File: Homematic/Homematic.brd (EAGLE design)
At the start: 99.2 x 85 mm, 28 parts, among them IC1 3.3V, IC2 3.3V, P1 DF11-06-2DS, Q1 BS170

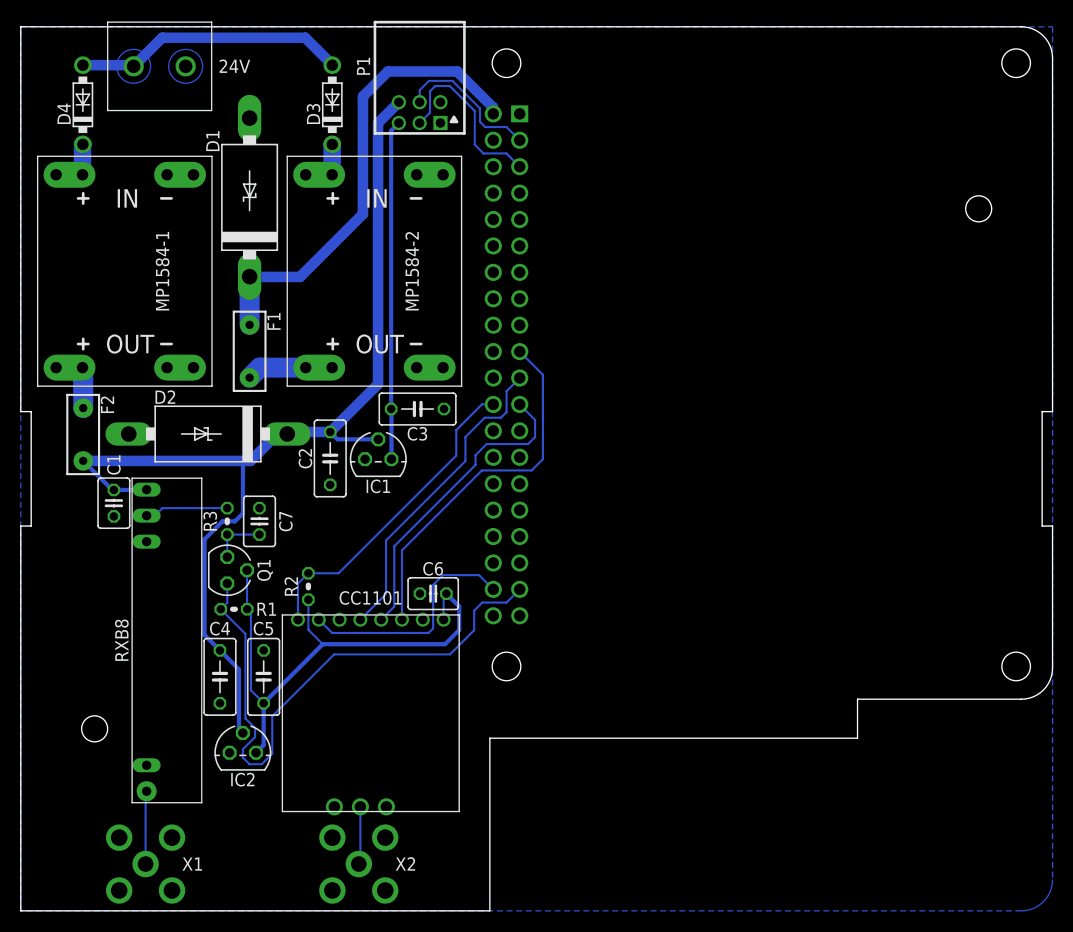
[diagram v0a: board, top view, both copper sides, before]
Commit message: Replace package for CC1101 receiver
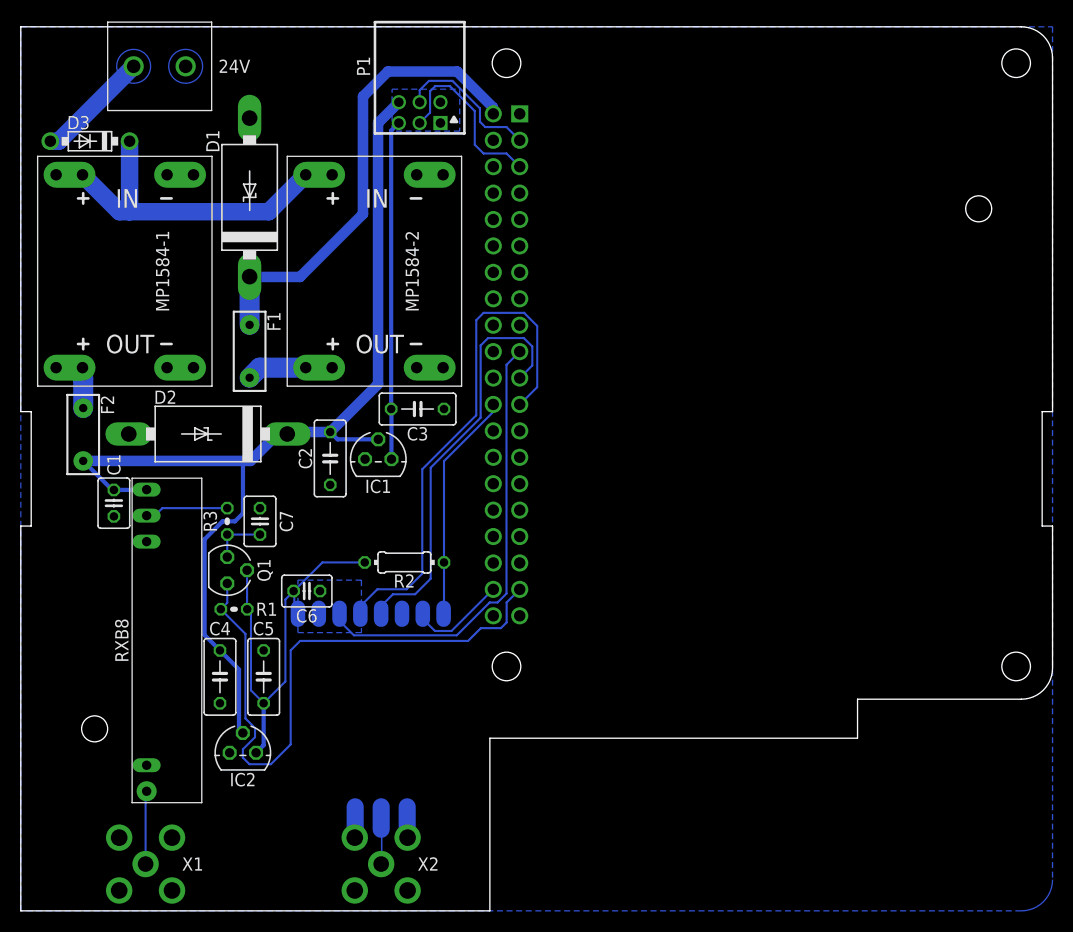
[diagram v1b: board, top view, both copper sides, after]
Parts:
- removed D4: SB1H100, diode:DO41-7.6
- CC1101: value CC1101 -> CC1101SMD; device modules:CC1101 -> modules:CC1101-SMD
- D3: value SB1H100 -> SB2H100
- R2: device rcl:0204V -> rcl:0204/7
- moved D3 23.6 mm to (6.65, 72.5), turned to 180 degrees
- moved C6 12.2 mm to (27.5, 29.2), turned to 0 degrees
- moved R2 9.51 mm to (36.9, 32.0), turned to 180 degrees
- moved X2 2.15 mm to (34.6, 3.00)
- moved C7 0.05 mm to (23.0, 36.0)
- flipped CC1101 to the bottom
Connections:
- removed net N$9: D4.C, MP1584-1.IN+0, MP1584-1.IN+1
- net +24V: no longer D4.A
- net N$7: now also MP1584-1.IN+0, MP1584-1.IN+1
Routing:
- net N$7: track 2.92 -> 31.2 mm
- net N$16: track 29.8 -> 49.5 mm
- net +24V: track 26.3 -> 11.0 mm
- net N$19: track 22.6 -> 9.49 mm
- net +3V3: track 51.7 -> 41.5 mm
- net N$17: track 30.5 -> 40.2 mm
- net N$15: track 30.8 -> 22.2 mm
- net N$18: track 35.1 -> 42.9 mm
- net N$10: track 55.9 -> 59.1 mm
- net N$9: track 2.93 -> 0.00 mm
- net N$20: track 5.56 -> 4.51 mm

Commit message: Change some routes
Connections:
- net N$10: now also RPI.40; no longer RPI.37
- net N$19: now also RPI.32; no longer RPI.38
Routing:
- net N$16: track 49.5 -> 40.9 mm
- net N$19: track 9.49 -> 17.3 mm
- net N$18: track 42.9 -> 48.2 mm
- net N$10: track 59.1 -> 54.0 mm
- net N$17: track 40.2 -> 37.1 mm
- net +3V3: track 41.5 -> 43.8 mm

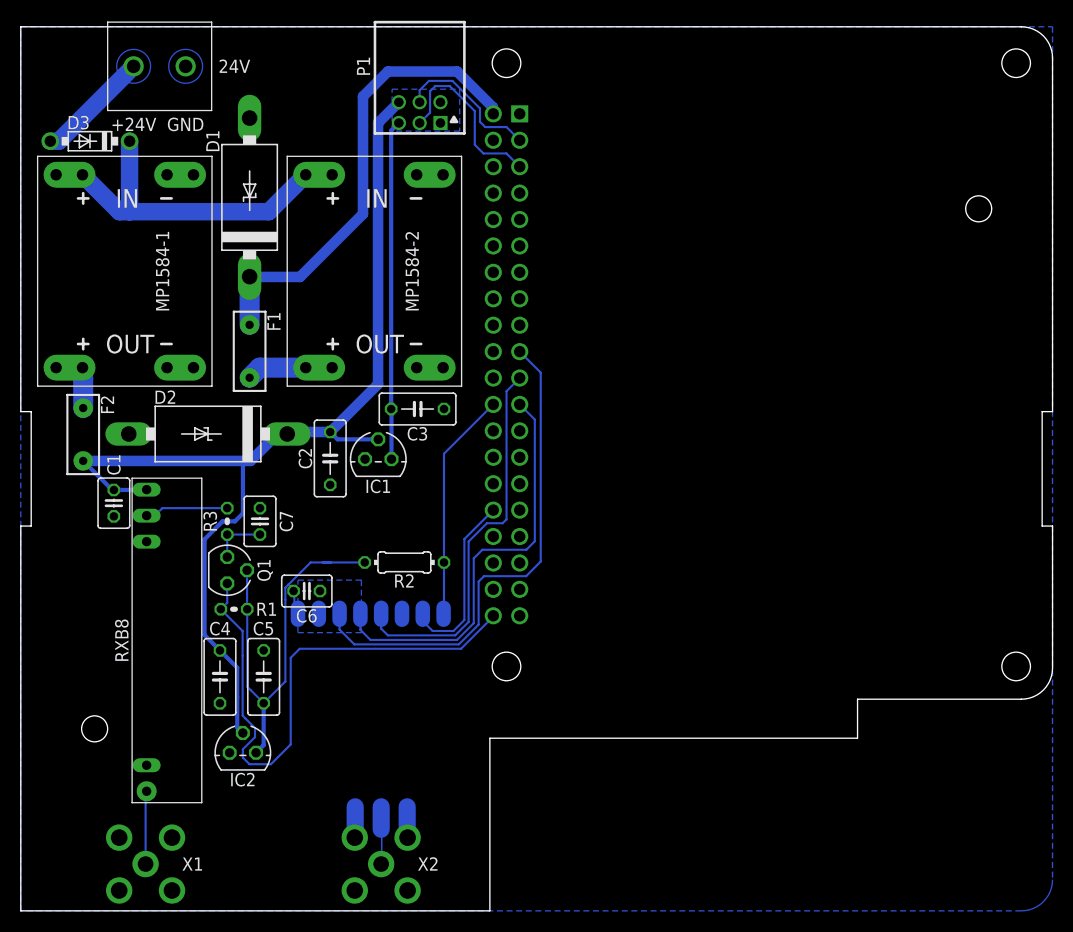
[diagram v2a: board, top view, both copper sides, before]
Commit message: Add top ground plate.
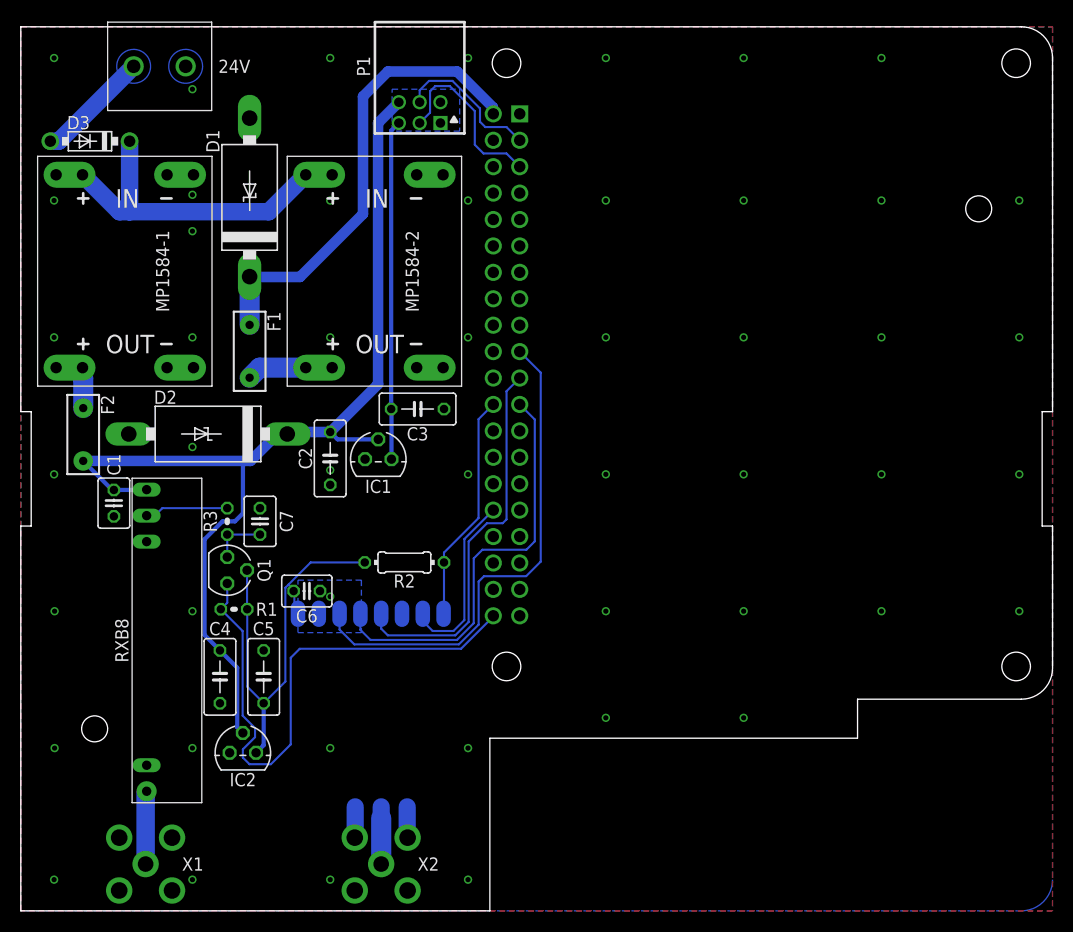
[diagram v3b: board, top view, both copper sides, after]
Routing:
- net +3V3: track 43.8 -> 42.9 mm
- added copper zone on layer 1, net GND

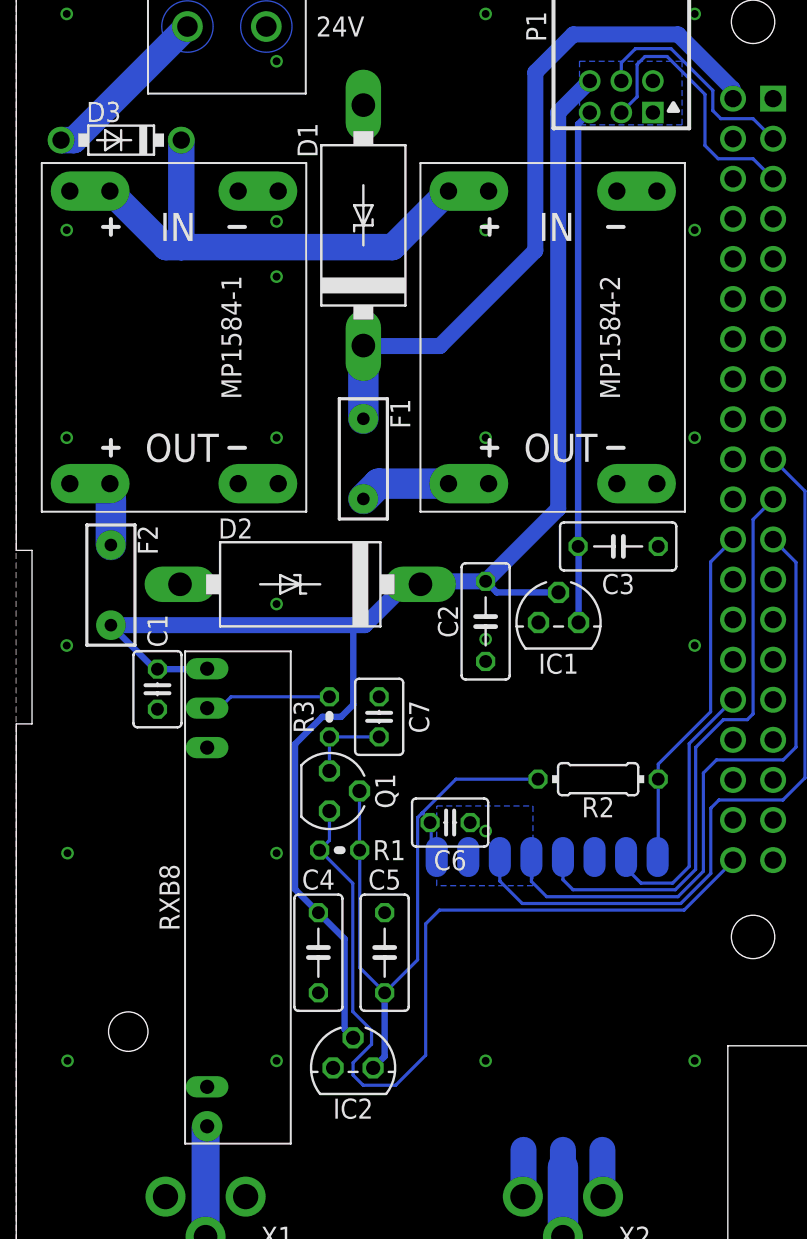
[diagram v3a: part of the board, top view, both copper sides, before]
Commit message: Replace trough hole capacitors with smd
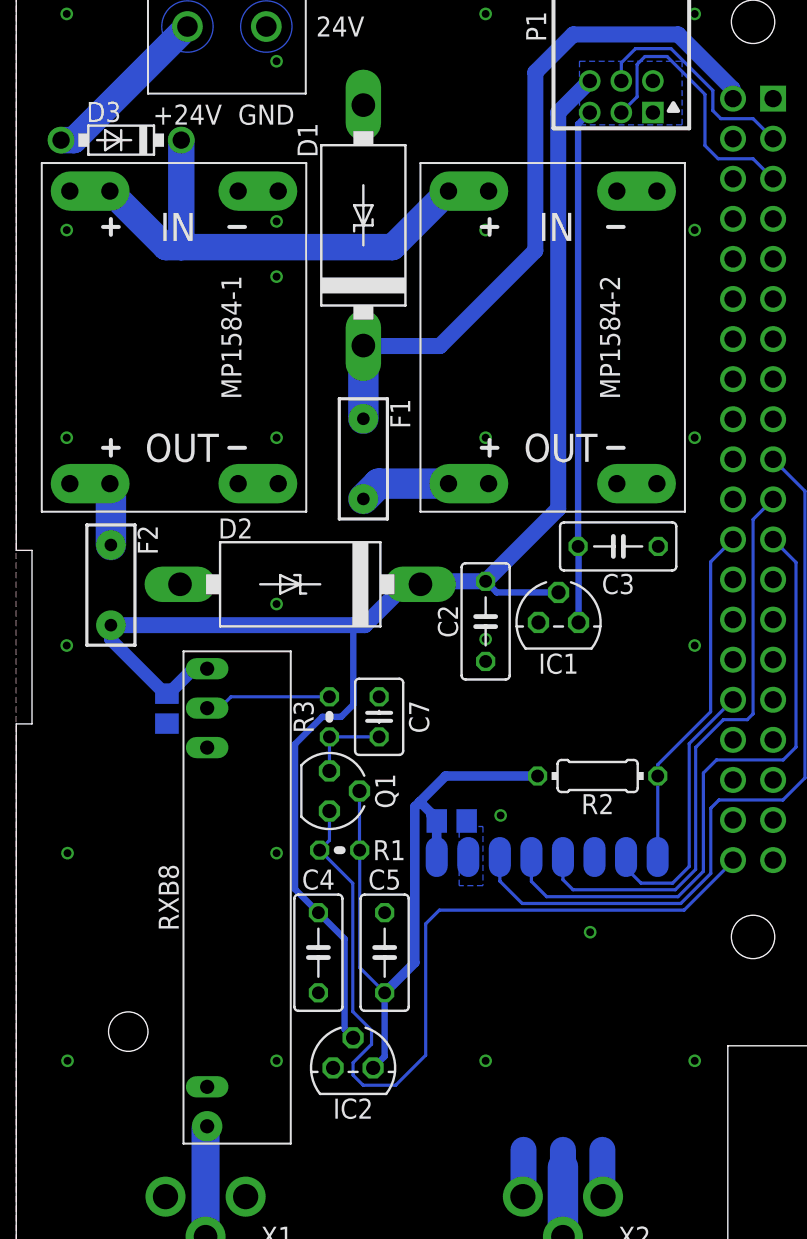
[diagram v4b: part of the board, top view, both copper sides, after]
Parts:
- C1, C6: device capacitor-wima:C2.5-3 -> rcl:C0805
- moved C1 1.37 mm to (9.55, 36.5), flipped to the bottom
- moved R2 0.20 mm to (36.9, 32.2)
- moved C6 0.14 mm to (27.6, 29.4), flipped to the bottom, turned to 180 degrees
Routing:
- net +5V: track 101.5 -> 103.3 mm
- net +3V3: track 42.9 -> 44.7 mm
